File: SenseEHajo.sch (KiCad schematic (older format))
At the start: 77 parts, among them IC1 AP3012, IC2 MCP3221, IC3 SN74AUP1G08-Q1, J1 Conn_01x02_Male, J2 REED, J3 RTC ( DS3231), J4 Heizung, J5 Pumpe, J6 Conn_01x05, J7 L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

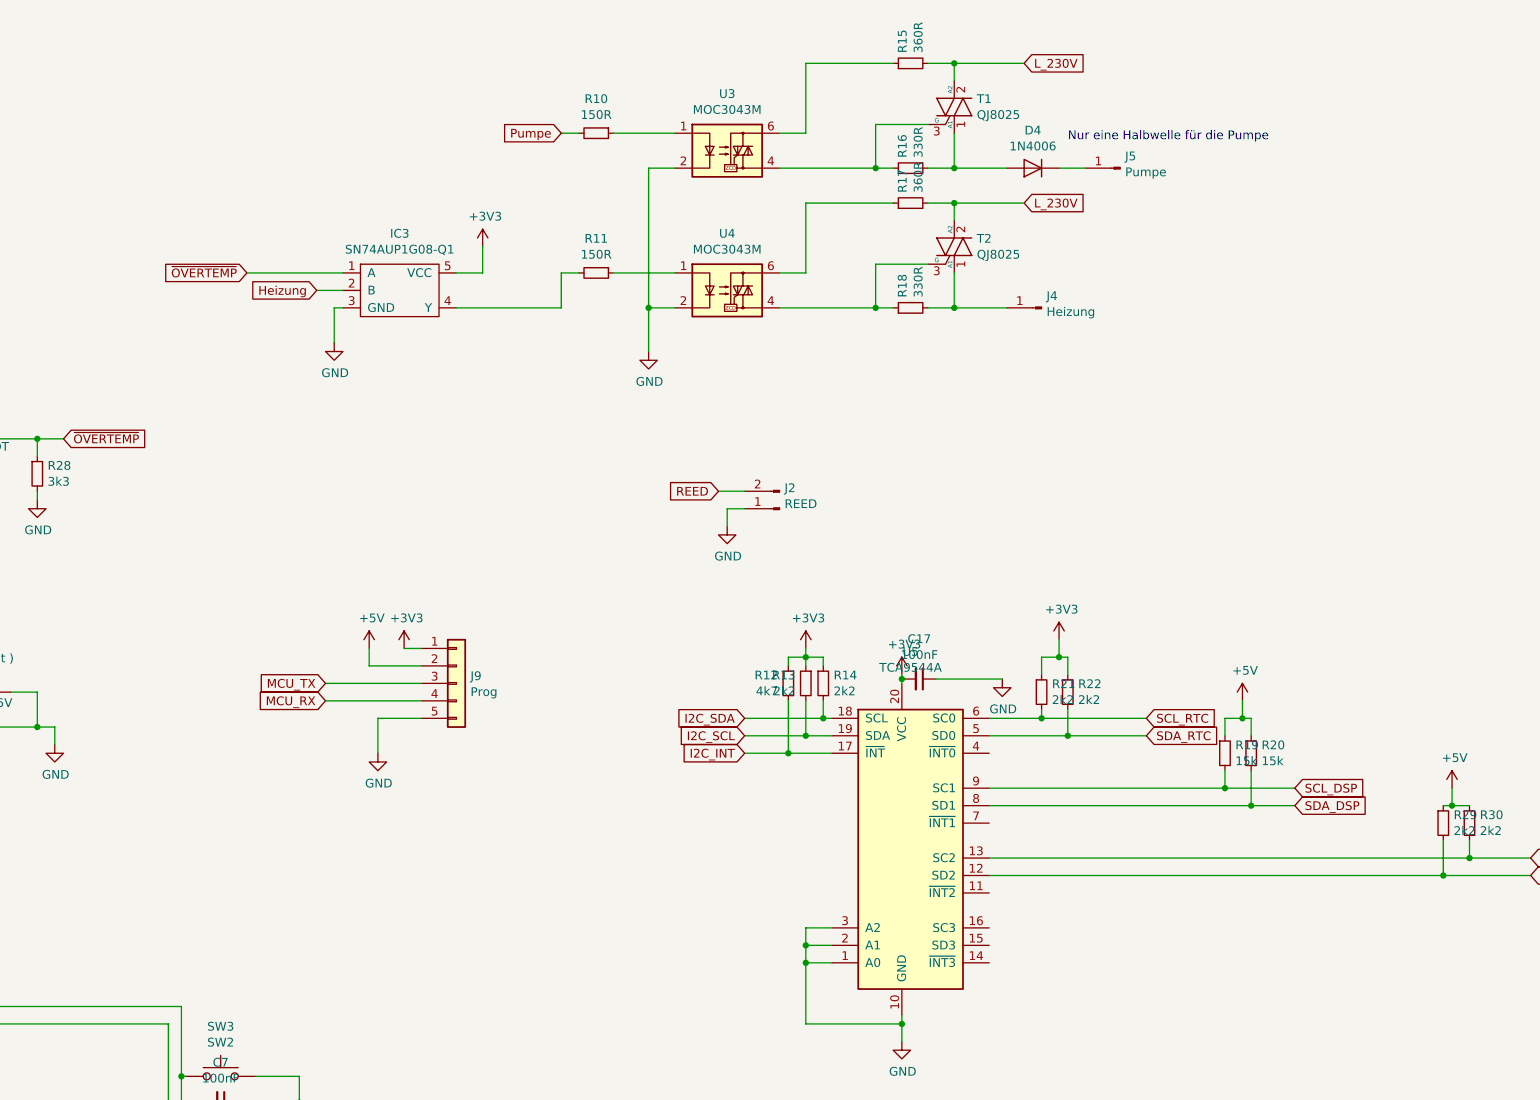
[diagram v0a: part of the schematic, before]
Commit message: Added Netfrequency Detection
This will detect the Netfrequency on IO25 of the ESP32. This is usefull to determine the amount of water pumped to the cup
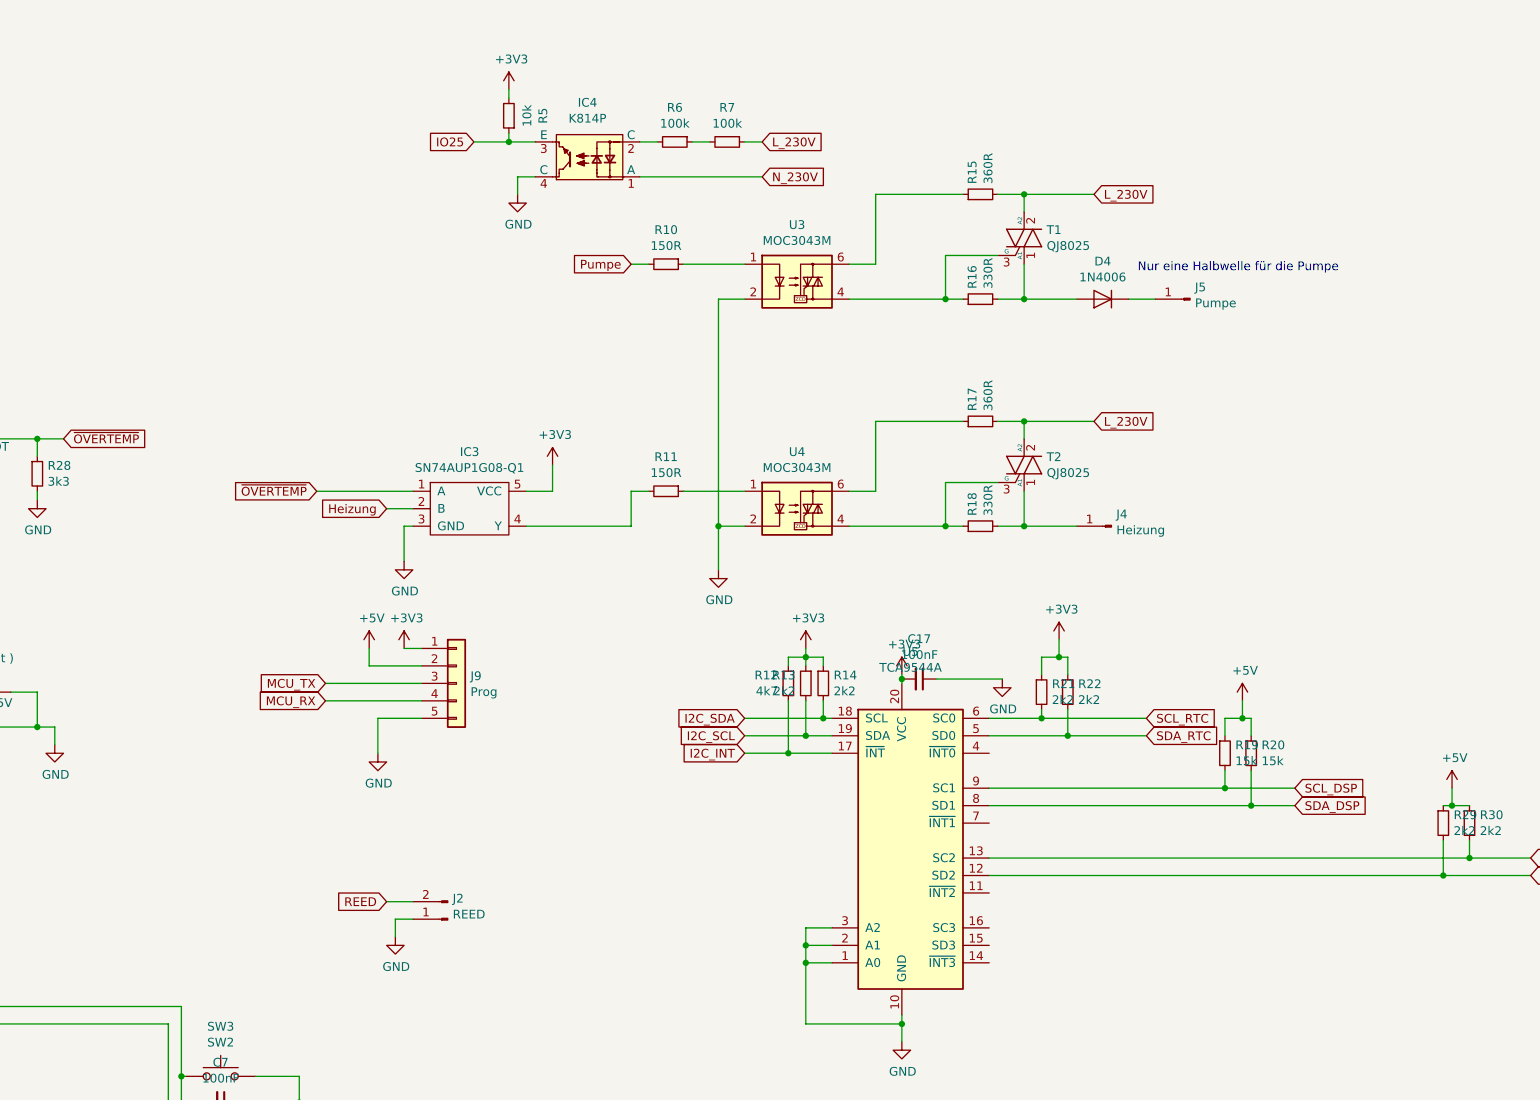
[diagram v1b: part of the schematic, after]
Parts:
- added IC4: K814P, Package_DIP:DIP-4_W7.62mm, symbol Vishay:K814P
- added R5: 10k, Resistor_SMD:R_0805_2012Metric_Pad1.15x1.40mm_HandSolder, symbol Device:R_Small
- added R6, R7: 100k, Resistor_THT:R_Axial_DIN0207_L6.3mm_D2.5mm_P7.62mm_Horizontal, symbol Device:R_Small
- C18, C19: footprint (none) -> Capacitor_SMD:C_0805_2012Metric_Pad1.15x1.40mm_HandSolder
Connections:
- net +3V3: now also R5.2
- net GND: now also IC4.4 (C)
- net IO25: now also IC4.3 (E), R5.1
- net L_230V: now also R7.1
- net N_230V: now also IC4.1 (A)
- new net: R6.1, R7.2
- new net: IC4.2 (C), R6.2
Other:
- moved on the sheet: D4, IC3, J2, J4, J5, R10, R11, R15, R16, R17, R18, T1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

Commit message: Version3
Ordered Proto for Version 3
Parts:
- C1, C14, C15, C16, C17, C19, C6, C7, C8: Order No. Mouser (none) -> 710-885012207098
- C10, C12: Order No. Mouser (none) -> 963-TMK212B7105KG-T
- C11: value 100uF -> 47uF/10V; Order No. Mouser (none) -> LMK316BC6476ML-T
- C13: Order No. Mouser (none) -> TMK212BBJ106KG-T
- C18, C4: Order No. Mouser (none) -> 0805X106K250CT
- C2: value 100nf / 10V -> 100nF / 10V; Order No. Mouser (none) -> 710-885012207098
- C3: Order No. Mouser (none) -> 80-C0805C105Z4V
- C5: value 100nF -> 100nF / 10V; Order No. Mouser (none) -> 710-885012207098
- C9: value 10uF -> 10uF/10V; Order No. Mouser (none) -> 710-885012107010
- D5: Order No. Mouser (none) -> 841-PMEG4010EGWX
- FB1: Order No. Mouser (none) -> 710-742792093
- IC1: Order No. Mouser (none) -> 621-AP3012KTR-G1
- IC2: Order No. Farnell (none) -> 1332098; Order No. Mouser (none) -> 579-MCP3221A5T-E/OT
- IC3: Order No. Mouser (none) -> 595-SN74AUP1G08DBVR
- IC4: Order No. Mouser (none) -> 782-K814P
- L1: Order No. Mouser (none) -> 710-74438335100
- R1, R4: Order No. Mouser (none) -> CRCW080510K0FKEAC
- R11: Order No. Mouser (none) -> CRCW0805150KFKEA
- R12, R24: Order No. Mouser (none) -> CRCW08054K70FKEBC
- R13, R14, R21, R22: Order No. Mouser (none) -> CRCW08052K20FKEAC
- R15, R17: Order No. Mouser (none) -> 71-CCF07360KGKE36
- R16: Order No. Mouser (none) -> CCF07330RJKE36
- R18: Order No. Mouser (none) -> 71-CCF07330RJKE36
- R19, R20: Order No. Mouser (none) -> CRCW080515K0FKEBC
- R2, R29, R30: Order No. Mouser (none) -> 71-CRCW08052K20FKEAC
- R23: Order No. Mouser (none) -> CRCW080539K0FKEAC
- R25: Order No. Mouser (none) -> 71-CRCW08051K00FKEAC
- R26: Order No. Mouser (none) -> 71-CRCW0805-3.92K-E3
- R27, R3: Order No. Mouser (none) -> 71-CRCW0805-1.8K-E3
- R28: Order No. Mouser (none) -> 71-CRCW08053K30FKEAC
- R5: Order No. Mouser (none) -> 71-CRCW080510K0FKEAC
- R6, R7: Order No. Mouser (none) -> 603-MFR-25FBF52-100K
- T2: Order No. Mouser (none) -> 576-QJ8025NH4RP
- U2: Order No. Farnell (none) -> 4974992; Order No. Mouser (none) -> 579-MCP6001T-I/OT
- U3, U4: Order No. Mouser (none) -> 512-MOC3043M
- U5: Order No. Mouser (none) -> 595-TCA9544APWR
- U6: Order No. Mouser (none) -> 926-LM1117MPX3.3NOPB
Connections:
- net GND: now also IC4.3 (E); no longer IC4.4 (C)
- net IO25: now also IC4.4 (C); no longer IC4.3 (E)
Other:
- note added: "In Revision 1 \nPins 3 and 4 are swapped\nso it is not working as intended\nIC must be placed at the bottom"
- moved on the sheet: R5, R6, R7
